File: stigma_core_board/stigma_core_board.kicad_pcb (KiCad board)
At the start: 4 copper layers, 40 x 40 mm, 93 parts, among them J1 TC2050, J3 CONN PLUG 70POS SMD GOLD, J5 USB_C_Receptacle_USB2.0, SW1 KMR721NGLFS, SW2 KMR721NGLFS, U1 STM32H743VITx, U10 H3LIS331DL, U11 MS5607/MS5611, U12 LIS3MDL, U13 BMP580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

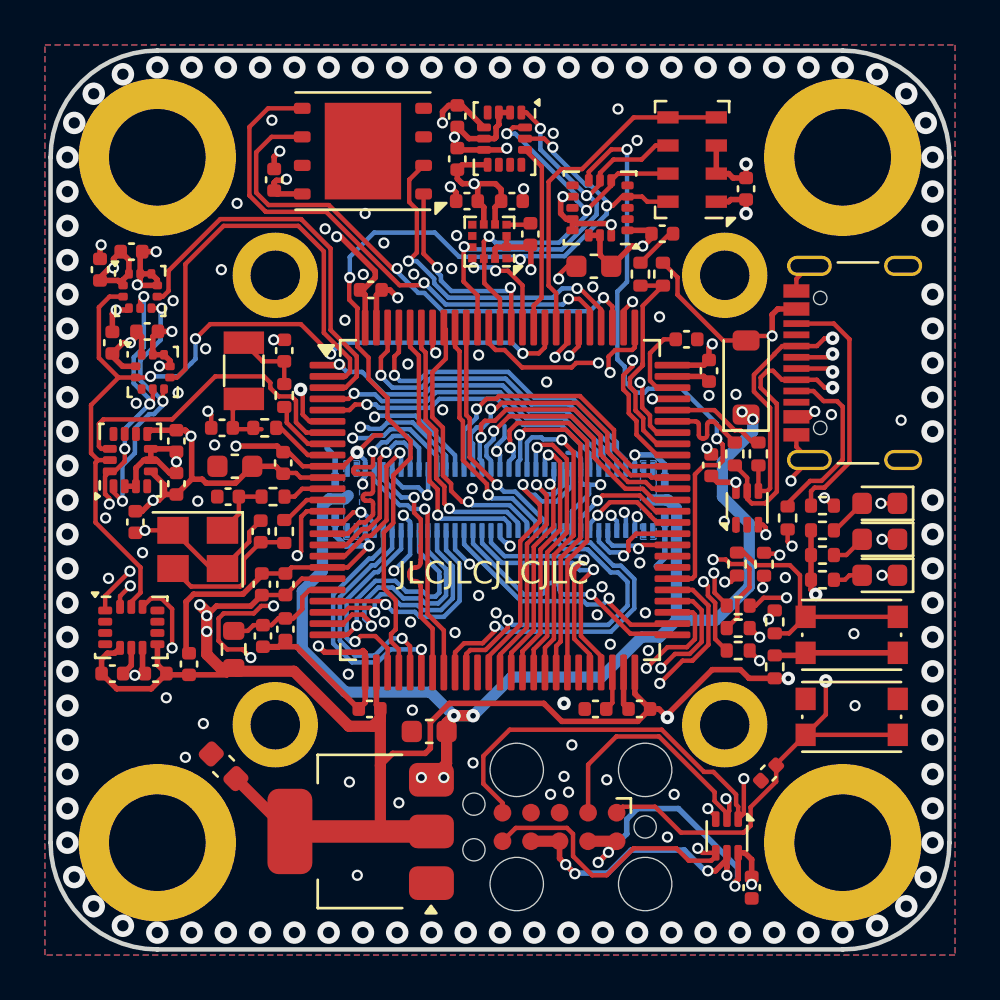
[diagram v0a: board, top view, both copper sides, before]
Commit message: core: Handle DRC warnings
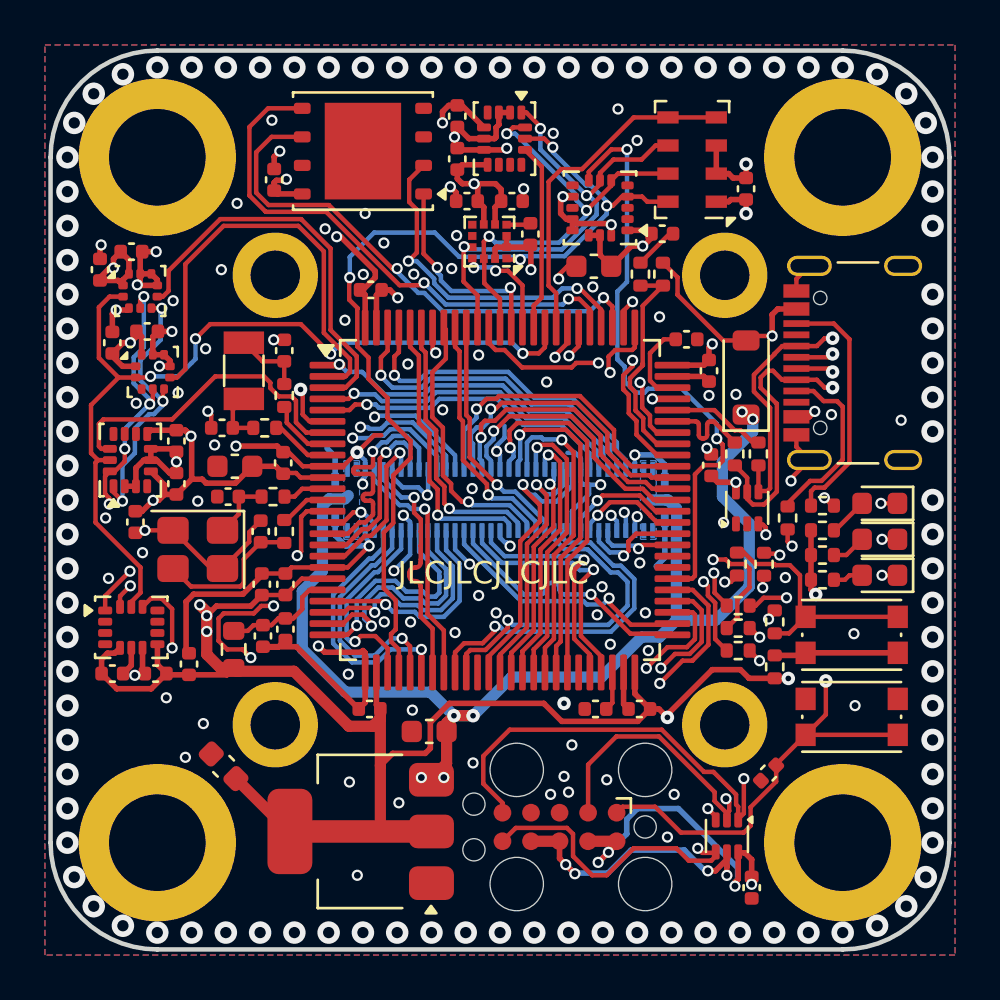
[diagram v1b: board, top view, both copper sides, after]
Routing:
- net unconnected-(U2-IO1-Pad1): track 0.51 -> 0.00 mm

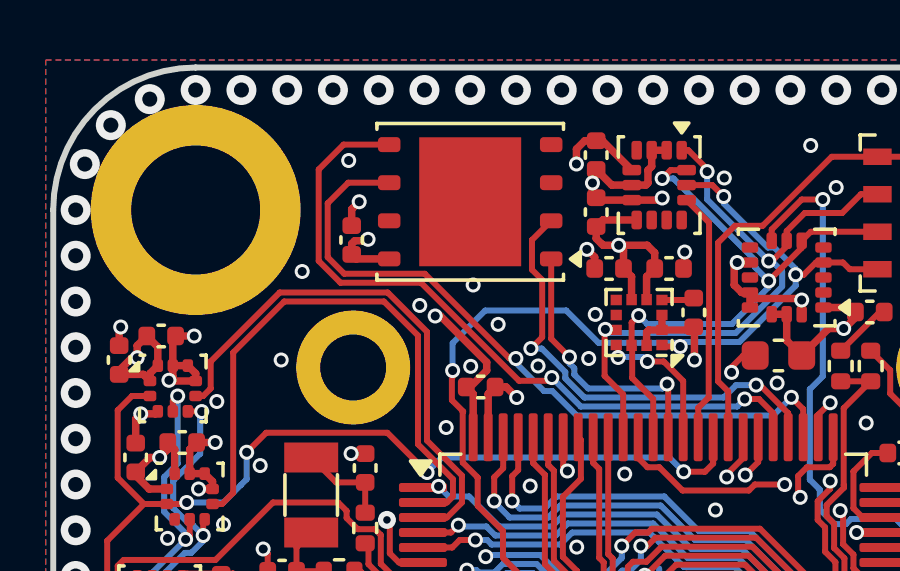
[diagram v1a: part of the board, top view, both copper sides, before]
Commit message: core: Replace flash w/ W25Q256, WSON 8x6
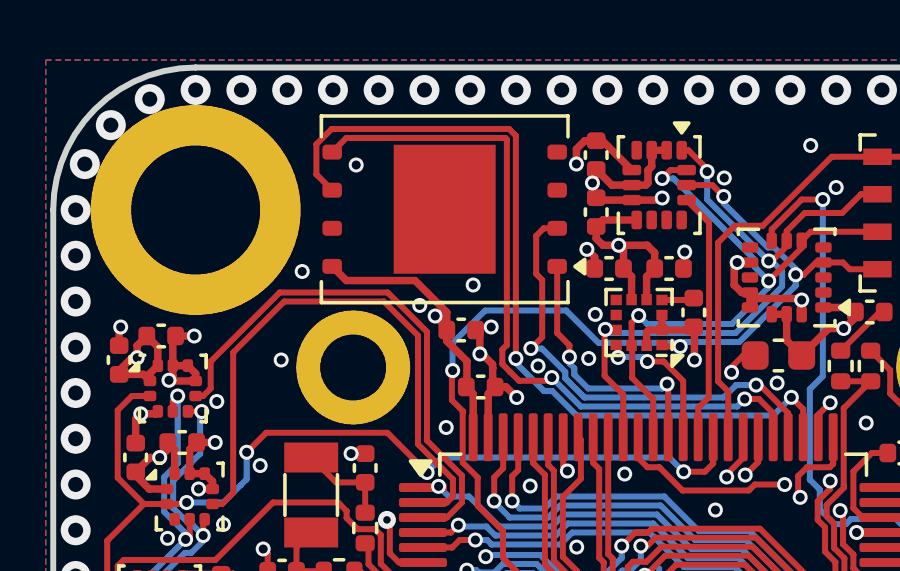
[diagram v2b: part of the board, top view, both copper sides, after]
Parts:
- U8: value W25Q128JVP -> W25Q256JVEIQ; footprint Package_SON:WSON-8-1EP_6x5mm_P1.27mm_EP3.4x4.3mm -> Package_SON:WSON-8-1EP_8x6mm_P1.27mm_EP3.4x4.3mm
- moved C20 4.72 mm to (108.8, 104.0), turned to 180 degrees
- moved U8 0.89 mm to (108.3, 100.0)
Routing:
- net SPI3_SCK: track 39.5 -> 43.8 mm
- net +3.3V: track 231.6 -> 233.8 mm, vias 22 -> 21
- net GND: track 123.4 -> 124.8 mm, vias 203 -> 202

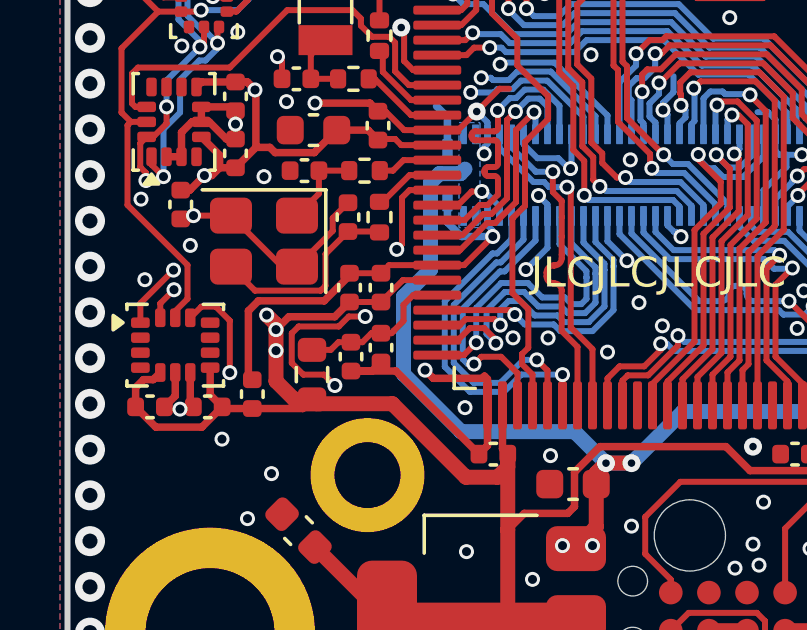
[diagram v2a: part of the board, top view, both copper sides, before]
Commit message: core: Connect VREF to VDDA
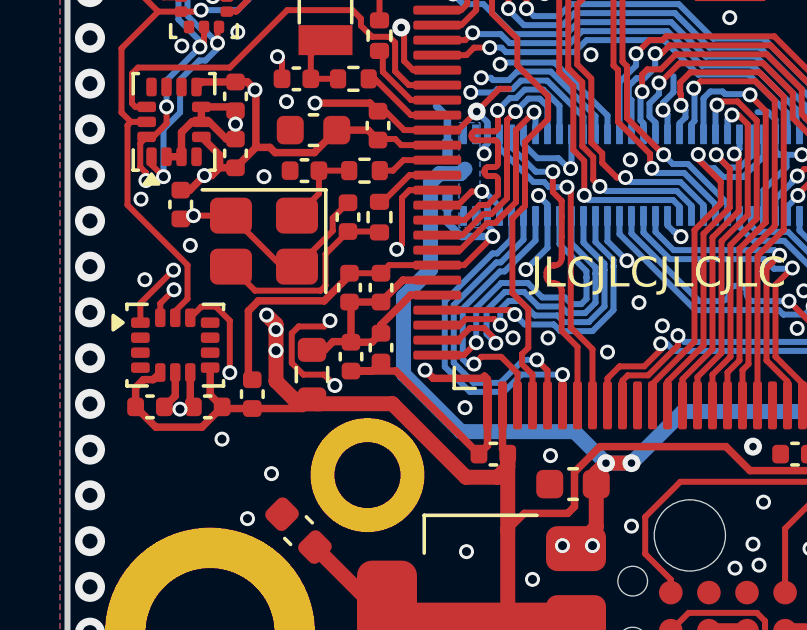
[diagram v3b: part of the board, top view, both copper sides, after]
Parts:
- U1: value STM32H743VITx -> STM32H743VIT6
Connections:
- C2 pad 1: +3.3V -> +3.3VA
- C4 pad 1: +3.3V -> +3.3VA
- U1 pad 20: +3.3V -> +3.3VA
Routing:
- net +3.3V: track 233.8 -> 227.7 mm
- net +3.3VA: track 5.25 -> 9.70 mm
- net Net-(U1-NRST): track 44.1 -> 43.4 mm
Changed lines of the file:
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@@
 			(layers "F.Cu" "F.Mask" "F.Paste")
 			(roundrect_rratio 0.25)
-			(net 16 "+3.3V")
+			(net 64 "+3.3VA")
 			(pintype "passive")
 		)
@@
 			(layers "F.Cu" "F.Mask" "F.Paste")
 			(roundrect_rratio 0.25)
-			(net 16 "+3.3V")
+			(net 64 "+3.3VA")
 			(pintype "passive")
 		)
@@
 			)
 		)
-		(property "Value" "STM32H743VITx"
+		(property "Value" "STM32H743VIT6"
 			(at 0 9.42 0)
 			(layer "F.Fab")
@@
 			)
 		)
-		(property "Description" "subst. with 753"
+		(property "Description" ""
 			(at 0 0 0)
 			(unlocked yes)
@@
 			)
 		)
-		(property "LCSC" "C730183"
+		(property "LCSC" "C114409"
 			(at 0 0 0)
 			(unlocked yes)
@@
 			(layers "F.Cu" "F.Mask" "F.Paste")
 			(roundrect_rratio 0.25)
-			(net 16 "+3.3V")
+			(net 64 "+3.3VA")
 			(pinfunction "VREF+")
 			(pintype "input")
@@
 	)
 	(segment
-		(start 103.8 121.9)
-		(end 104.161023 122.261023)
+		(start 103.11 121.9)
+		(end 103.8 121.9)
 		(width 0.2)
 		(layer "F.Cu")
@@
 	)
 	(segment
-		(start 104.626917 119.962705)
-		(end 104.294622 120.295)
+		(start 102.725001 120.524999)
+		(end 102.725001 121.515001)
 		(width 0.2)
 		(layer "F.Cu")
@@
 	)
 	(segment
-		(start 104.161023 122.261023)
-		(end 104.161023 122.262791)
+		(start 103.805 120.295)
+		(end 102.955 120.295)
 		(width 0.2)
 		(layer "F.Cu")
@@
 	)
 	(segment
-		(start 104.294622 120.295)
-		(end 102.955 120.295)
-		(width 0.2)
-		(layer "F.Cu")
-		(net 3)
-	)
-	(segment
-		(start 126.95 119.143213)
-		(end 126.94157 119.151643)
+		(start 104.161023 122.261023)
+		(end 104.161023 122.262791)
 		(width 0.2)
 		(layer "F.Cu")
@@
 	)
 	(segment
-		(start 102.955 120.295)
-		(end 102.725001 120.524999)
+		(start 103.8 121.9)
+		(end 104.161023 122.261023)
 		(width 0.2)
 		(layer "F.Cu")
@@
 	)
 	(segment
-		(start 102.725001 120.524999)
-		(end 102.725001 121.515001)
+		(start 126.95 119.143213)
+		(end 126.94157 119.151643)
 		(width 0.2)
 		(layer "F.Cu")
@@
 	)
 	(segment
-		(start 105.174013 119.962705)
-		(end 104.626917 119.962705)
+		(start 102.955 120.295)
+		(end 102.725001 120.524999)
 		(width 0.2)
 		(layer "F.Cu")
@@
 	)
 	(segment
-		(start 103.11 121.9)
-		(end 103.8 121.9)
+		(start 107.575 115.75)
+		(end 106.65 115.75)
 		(width 0.2)
 		(layer "F.Cu")
@@
 	)
 	(segment
-		(start 107.575 115.75)
-		(end 106.65 115.75)
+		(start 102.725001 121.515001)
+		(end 103.11 121.9)
 		(width 0.2)
 		(layer "F.Cu")
@@
 	)
 	(segment
-		(start 102.725001 121.515001)
-		(end 103.11 121.9)
+		(start 104 120.1)
+		(end 103.805 120.295)
 		(width 0.2)
 		(layer "F.Cu")
@@
 	)
 	(via
-		(at 105.174013 119.962705)
+		(at 104 120.1)
 		(size 0.5)
 		(drill 0.3)
@@
 	)
 	(segment
-		(start 105.174013 118.375987)
-		(end 105.825 117.725)
-		(width 0.2)
-		(layer "In2.Cu")
-		(net 3)
-	)
-	(segment
 		(start 106.119849 127.35)
 		(end 104.380151 127.35)
@@
 	)
 	(segment
-		(start 103.15 124.380151)
-		(end 104.161023 123.369128)
+		(start 105.825 117.725)
+		(end 106.225 117.725)
 		(width 0.2)
 		(layer "In2.Cu")
@@
 	)
 	(segment
-		(start 105.174013 119.962705)
-		(end 105.174013 118.375987)
+		(start 103.15 124.380151)
+		(end 104.161023 123.369128)
 		(width 0.2)
 		(layer "In2.Cu")
@@
 	)
 	(segment
+		(start 104 120.1)
+		(end 105.174013 118.925987)
+		(width 0.2)
+		(layer "In2.Cu")
+		(net 3)
+	)
+	(segment
 		(start 106.969849 126.5)
 		(end 106.119849 127.35)
@@
 	)
 	(segment
-		(start 105.825 117.725)
-		(end 106.225 117.725)
+		(start 105.174013 118.375987)
+		(end 105.825 117.725)
+		(width 0.2)
+		(layer "In2.Cu")
+		(net 3)
+	)
+	(segment
+		(start 105.174013 118.925987)
+		(end 105.174013 118.375987)
 		(width 0.2)
 		(layer "In2.Cu")
@@
 	)
 	(segment
-		(start 102.63 119.97)
-		(end 104.160002 119.97)
-		(width 0.25)
-		(layer "F.Cu")
-		(net 16)
-	)
-	(segment
 		(start 116.63 130.435)
 		(end 117.9 130.435)
@@
 	)
 	(segment
-		(start 106.43 118.750002)
-		(end 105.7 119.48)
-		(width 0.2)
-		(layer "F.Cu")
-		(net 16)
-	)
-	(segment
 		(start 125.350001 131.550001)
 		(end 125.350001 130.95)
@@
 	)
 	(segment
-		(start 102.2 120.4)
-		(end 102.63 119.97)
-		(width 0.25)
-		(layer "F.Cu")
-		(net 16)
-	)
-	(segment
 		(start 109.925 124.55)
 		(end 109.925 127.075)
@@
 	)
 	(segment
-		(start 107.575 118.750001)
-		(end 106.43 118.750002)
-		(width 0.2)
-		(layer "F.Cu")
-		(net 16)
-	)
-	(segment
 		(start 105.85 130)
 		(end 103.498008 127.648008)
@@
 	)
 	(segment
-		(start 104.160002 119.97)
-		(end 104.650001 119.480001)
-		(width 0.25)
-		(layer "F.Cu")
-		(net 16)
-	)
-	(segment
 		(start 122.325523 124.55)
 		(end 121.93 124.55)
@@
 	)
 	(segment
-		(start 105.7 119.48)
-		(end 104.65 119.480002)
-		(width 0.2)
-		(layer "F.Cu")
-		(net 16)
-	)
-	(segment
 		(start 114.26 101.95)
 		(end 114.26 101.335)
@@
 	)
 	(segment
-		(start 104.024999 121.075)
-		(end 103.400001 121.075)
-		(width 0.2)
+		(start 105.7 119.480001)
+		(end 106.430001 118.75)
+		(width 0.25)
 		(layer "F.Cu")
 		(net 64)
 	)
 	(segment
-		(start 104.7 120.820001)
-		(end 104.28 120.820001)
-		(width 0.2)
+		(start 104.7 120.820002)
+		(end 105.399999 120.820002)
+		(width 0.25)
 		(layer "F.Cu")
 		(net 64)
 	)
 	(segment
-		(start 106.45 119.575004)
-		(end 106.45 120.110001)
-		(width 0.2)
+		(start 104.7 120.820002)
+		(end 104.7 119.53)
+		(width 0.25)
 		(layer "F.Cu")
 		(net 64)
 	)
 	(segment
-		(start 105.7 120.520002)
-		(end 105.38 120.520002)
-		(width 0.2)
+		(start 103.400001 121.075)
+		(end 103.825 121.075)
+		(width 0.25)
 		(layer "F.Cu")
 		(net 64)
 	)
 	(segment
-		(start 105.08 120.820002)
-		(end 104.7 120.820001)
-		(width 0.2)
+		(start 104.650001 119.480001)
+		(end 105.7 119.480001)
+		(width 0.25)
 		(layer "F.Cu")
 		(net 64)
 	)
 	(segment
-		(start 104.28 120.820001)
-		(end 104.024999 121.075)
-		(width 0.2)
+		(start 106.690002 119.25)
+		(end 107.575 119.25)
+		(width 0.25)
 		(layer "F.Cu")
 		(net 64)
 	)
 	(segment
-		(start 106.13 120.44)
-		(end 106.050001 120.52)
-		(width 0.2)
+		(start 106.430001 118.75)
+		(end 107.575 118.75)
+		(width 0.25)
 		(layer "F.Cu")
 		(net 64)
 	)
 	(segment
-		(start 106.775001 119.250001)
-		(end 106.45 119.575004)
-		(width 0.2)
+		(start 103.825 121.075)
+		(end 104.1 120.8)
+		(width 0.25)
 		(layer "F.Cu")
 		(net 64)
 	)
 	(segment
-		(start 107.575 119.250002)
-		(end 106.775001 119.250001)
-		(width 0.2)
+		(start 105.7 120.520001)
+		(end 105.7 120.240002)
+		(width 0.25)
 		(layer "F.Cu")
 		(net 64)
 	)
 	(segment
-		(start 105.38 120.520002)
-		(end 105.08 120.820002)
-		(width 0.2)
+		(start 104.1 120.8)
+		(end 104.679998 120.8)
+		(width 0.25)
 		(layer "F.Cu")
 		(net 64)
 	)
 	(segment
-		(start 106.050001 120.52)
-		(end 105.7 120.520002)
-		(width 0.2)
+		(start 104.679998 120.8)
+		(end 104.7 120.820002)
+		(width 0.25)
 		(layer "F.Cu")
 		(net 64)
 	)
 	(segment
-		(start 106.13 120.43)
-		(end 106.13 120.44)
-		(width 0.2)
+		(start 104.7 119.53)
+		(end 104.650001 119.480001)
+		(width 0.25)
 		(layer "F.Cu")
 		(net 64)
 	)
 	(segment
-		(start 106.45 120.110001)
-		(end 106.13 120.43)
-		(width 0.2)
+		(start 105.7 120.240002)
+		(end 106.690002 119.25)
+		(width 0.25)
+		(layer "F.Cu")
+		(net 64)
+	)
+	(segment
+		(start 105.399999 120.820002)
+		(end 105.7 120.520001)
+		(width 0.25)
 		(layer "F.Cu")
 		(net 64)

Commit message: core: Final bom changes, production files
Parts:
- R12, R13: value 22R -> 22
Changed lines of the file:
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@@
 			)
 		)
-		(property "LCSC" "C2297"
+		(property "LCSC" "C965804"
 			(at 0 0 180)
 			(unlocked yes)
@@
 			)
 		)
-		(property "Value" "22R"
+		(property "Value" "22"
 			(at 0 1.17 90)
 			(layer "F.Fab")
@@
 			)
 		)
-		(property "LCSC" "C28323"
+		(property "LCSC" "C52923"
 			(at 0 0 0)
 			(unlocked yes)
@@
 			)
 		)
-		(property "LCSC" "C28323"
+		(property "LCSC" "C52923"
 			(at 0 0 90)
 			(unlocked yes)
@@
 			)
 		)
-		(property "LCSC" "C28323"
+		(property "LCSC" "C52923"
 			(at 0 0 90)
 			(unlocked yes)
@@
 			)
 		)
-		(property "LCSC" "C28323"
+		(property "LCSC" "C52923"
 			(at 0 0 270)
 			(unlocked yes)
@@
 			)
 		)
-		(property "Value" "22R"
+		(property "Value" "22"
 			(at 0 1.17 90)
 			(layer "F.Fab")
@@
 			)
 		)
-		(property "LCSC" "C28323"
+		(property "LCSC" "C52923"
 			(at 0 0 270)
 			(unlocked yes)
@@
 			)
 		)
-		(property "LCSC" "C2296"
+		(property "LCSC" "C72038"
 			(at 0 0 180)
 			(unlocked yes)
@@
 			)
 		)
-		(property "Description" "populated manually"
+		(property "Description" ""
 			(at 0 0 0)
 			(unlocked yes)
@@
 		(sheetname "/")
 		(sheetfile "stigma_core_board.kicad_sch")
-		(attr smd exclude_from_bom)
+		(attr smd)
 		(fp_line
 			(start 7.58 -0.875)
